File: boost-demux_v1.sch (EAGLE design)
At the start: 0 parts

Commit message: Lib updates + boost-demux design
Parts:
- added C1, C2: 4.7u, rcl:C-USC1206
- added C3: 100n, rcl:C-USC1206
- added C4: 10n, rcl:C-USC1206
- added C5: 22n, rcl:C-USC1206
- added C6: 1.8n, rcl:C-USC0805
- added C7: 27n, rcl:C-USC0805
- added C8, C9: 10u, rcl:C-USC1206
- added D1: FAIRCHILD_FSV8100V, components:FAIRCHILD_FSV8100V
- added L1: 4.7U, components:MURATA_FDVE1040
- added R1: 47k, rcl:R-US_R1206
- added R2: 1.37k, rcl:R-US_R0805
- added R3: 10k, rcl:R-US_R0805
- added R4: 154k, rcl:R-US_R0805
- added U1: TI_TPS55330, components:TI_TPS55330
- added U2, U3: (no value), SparkFun-PowerIC:ULN2803SOICW
- added U4: 4067D, 40xx:4067D
- added X1: (no value), pinhead:PINHD-2X8
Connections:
- new net +12V: C1.1, C2.1, C3.1, C4.1, L1.1, U1.EN, U1.VIN
- new net GND: C1.2, C2.2, C3.2, C4.2, C5.2, C6.2, C7.2, C8.2, C9.2, R1.1, R3.1, U1.AGND, U1.PAD, U1.PGND
- new net N$1: R1.2, U1.FREQ
- new net N$2: C5.1, U1.SS
- new net N$3: C6.1, R2.1, U1.COMP
- new net N$4: C7.1, R2.2
- new net N$5: R3.2, R4.1, U1.FB
- new net N$6: C8.1, C9.1, D1.C, R4.2
- new net N$7: D1.A, L1.2, U1.SW

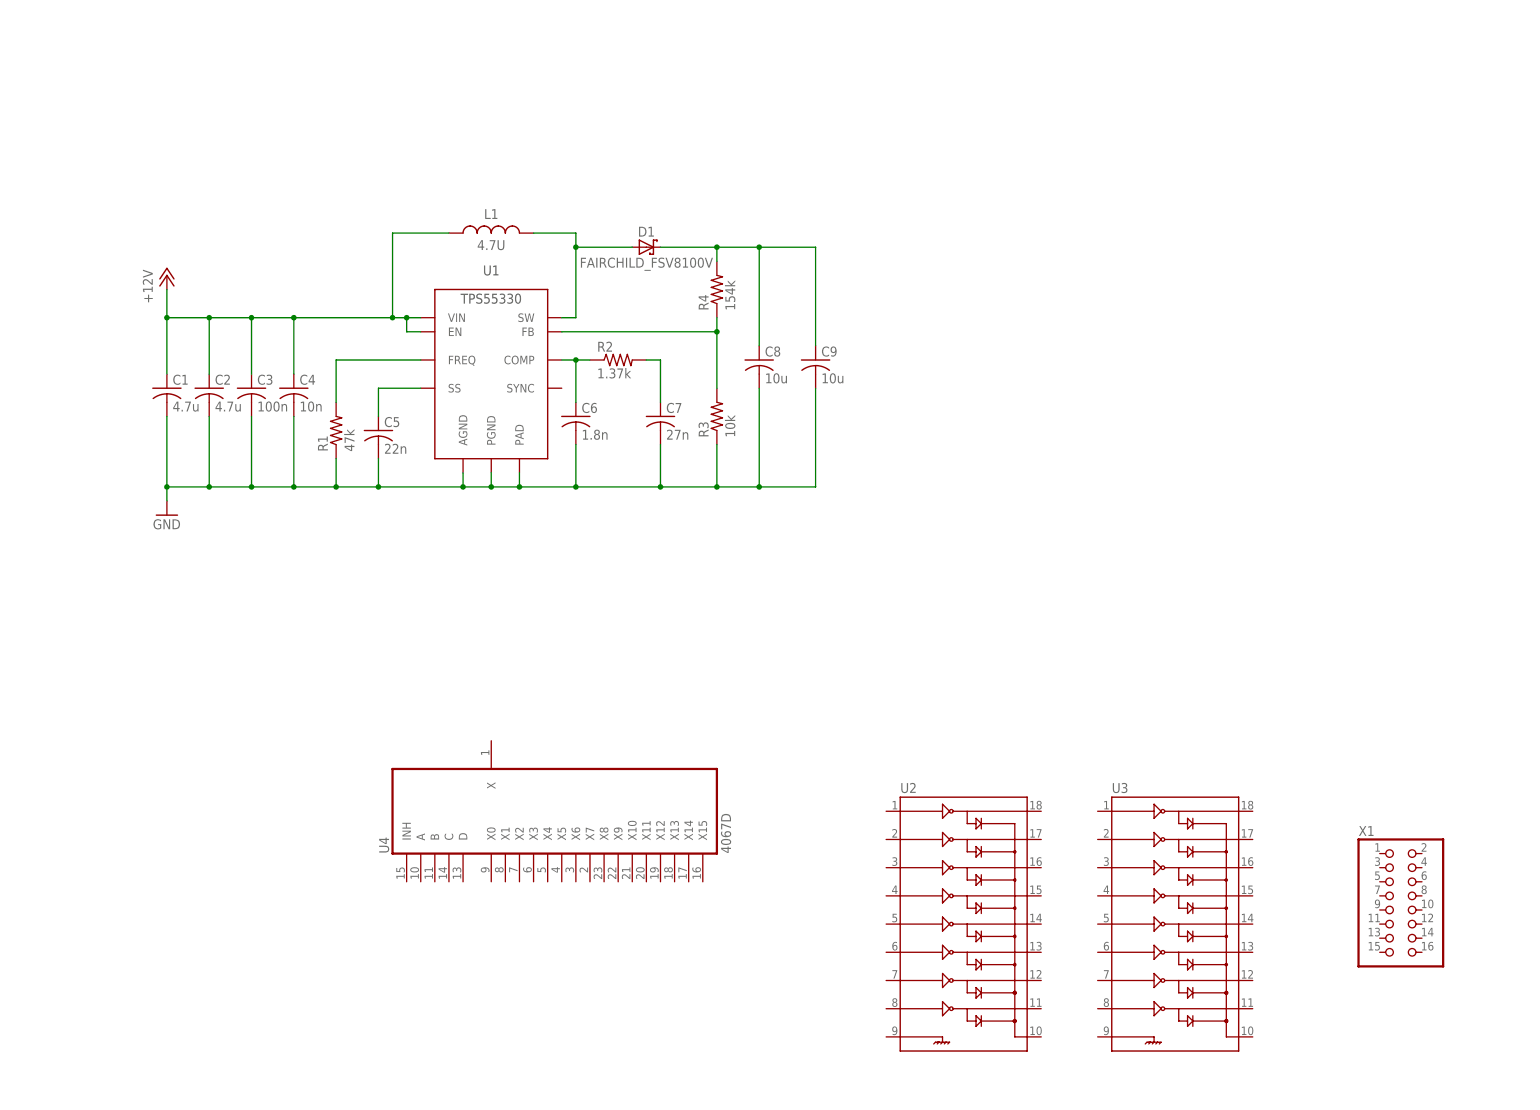
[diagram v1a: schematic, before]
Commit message: Slight update to boost-demux schematic
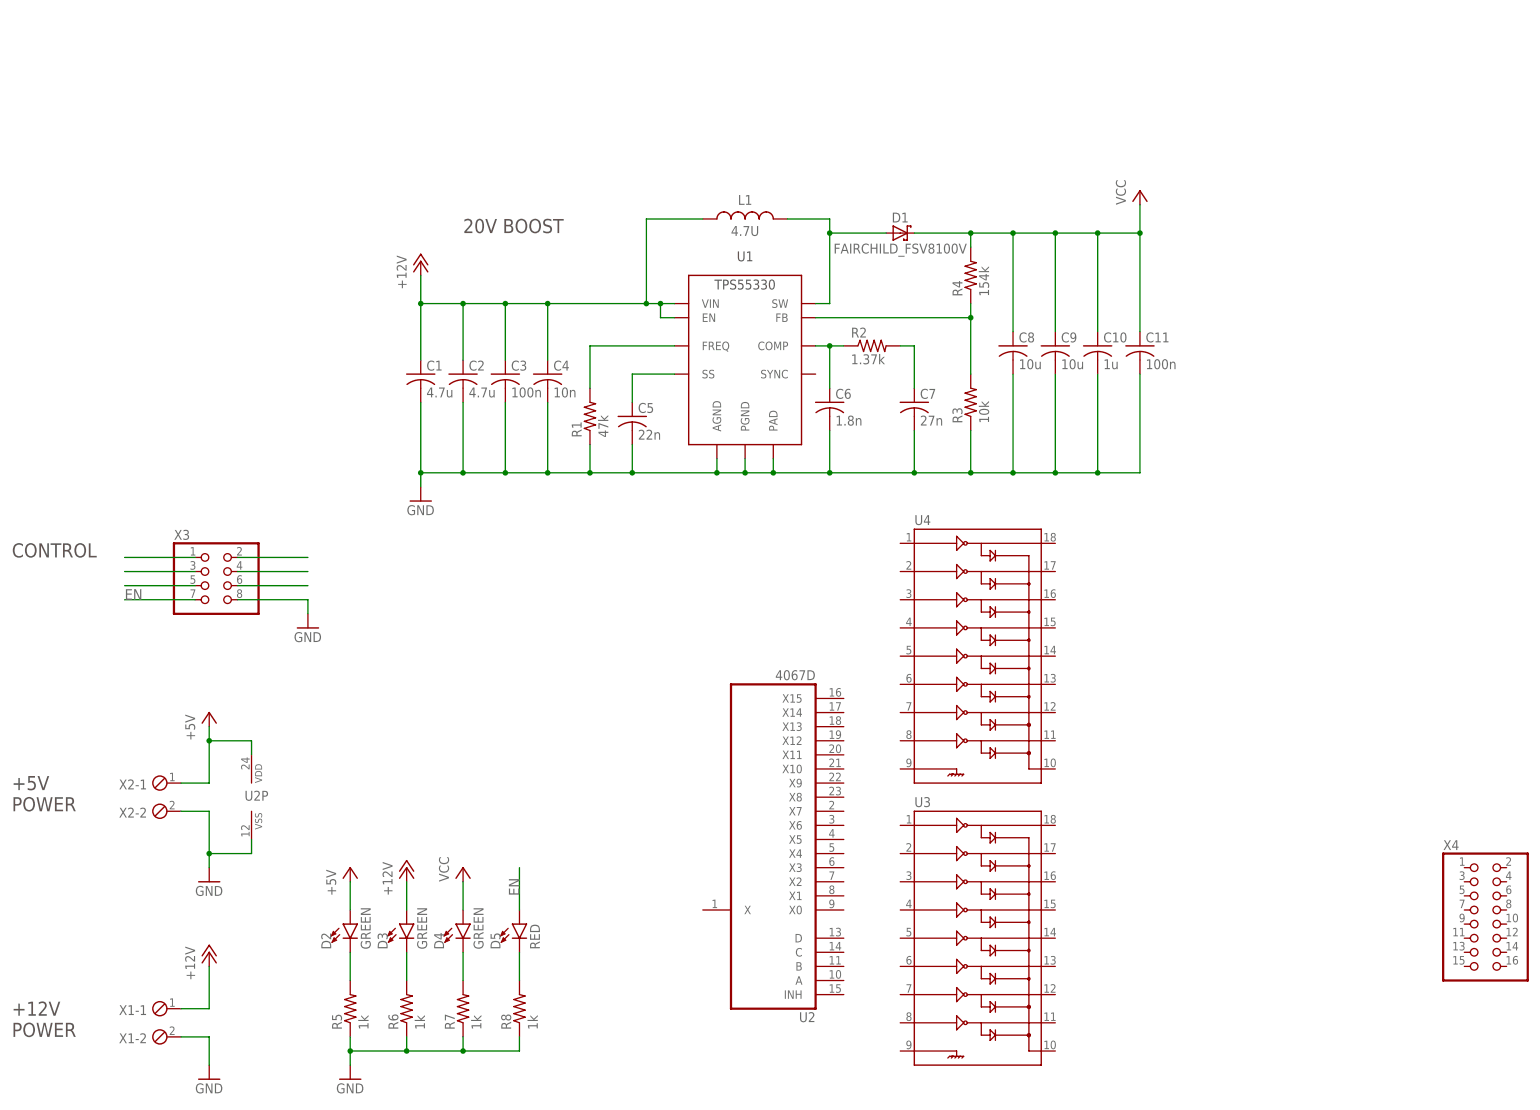
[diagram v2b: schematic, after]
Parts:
- added C10: 1u, rcl:C-USC1206
- added C11: 100n, rcl:C-USC1206
- added D2, D3, D4: GREEN, SparkFun-LED:LED5MM
- added D5: RED, SparkFun-LED:LED5MM
- added R5, R6, R7, R8: 1k, resistor:R-US_R1206
- added X2: (no value), con-phoenix-254:MPT2
- added X3: (no value), pinhead:PINHD-2X4/90
- added X4: (no value), pinhead:PINHD-2X8
- U2: value (none) -> 4067D; device SparkFun-PowerIC:ULN2803SOICW -> 40xx:4067D
- U4: value 4067D -> (none); device 40xx:4067D -> SparkFun-PowerIC:ULN2803SOICW
- X1: device pinhead:PINHD-2X8 -> con-phoenix-254:MPT2
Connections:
- new net +5V: D2.A, U2P.VDD, X2-1.1
- new net EN: D5.A, X3.7
- new net N$10: D5.C, R8.2
- new net N$11: X3.1
- new net N$14: X3.5
- new net N$15: X3.3
- new net N$16: X3.2
- new net N$17: X3.4
- new net N$18: X3.6
- new net N$8: D3.C, R6.2
- new net N$9: D4.C, R7.2
- new net VCC: C10.1, C11.1, C8.1, C9.1, D1.C, D4.A, R4.2
- net +12V: now also D3.A, X1-1.1
- net GND: now also C10.2, C11.2, R5.1, R6.1, R7.1, R8.1, U2P.VSS, X1-2.1, X2-2.1, X3.8
- net N$6: now also D2.C, R5.2; no longer C8.1, C9.1, D1.C, R4.2
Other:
- note added: "+12V POWER"
- note added: "+5V POWER"
- note added: "20V BOOST"
- note added: "CONTROL"
- moved on the sheet: C1, C2, C3, C4, C5, C6, C7, C8, C9, D1, L1, R1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

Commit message: PCB draft less markup
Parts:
- added C12: 100n, rcl:C-USC1206
- added D6: ON_FSV8100V, components:ON_FSV8100V
- added M1, M2, M3, M4: 6-32_MOUNT, components:6-32_MOUNT
- added Q1: ON_FDD4141, components:ON_FDD4141
- added R10, R11: 10k, rcl:R-US_R0805
- added R9: 470, resistor:R-US_R1206
- added U5: AVAGO_ACPL-217, components:AVAGO_ACPL-217
- added X5: (no value), pinhead:PINHD-2X8
- D1: value FAIRCHILD_FSV8100V -> ON_FSV8100V; device components:FAIRCHILD_FSV8100V -> components:ON_FSV8100V
- X2: device con-phoenix-254:MPT2 -> pinhead:PINHD-1X2/90
- X4: device pinhead:PINHD-2X8 -> pinhead:PINHD-1X3/90
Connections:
- new net A: U2A.A, X3.6
- new net B: U2A.B, X3.3
- new net C: U2A.C, X3.7
- new net D: U2A.D, X3.2
- new net N$12: C10.1, C11.1, C8.1, C9.1, D1.C, Q1.S, R10.1, R4.2
- new net N$13: Q1.G, R10.2, U5.P$4
- new net N$19: R9.1, U5.P$2
- new net N$20: U2A.X4, U3.4
- new net N$21: U2A.X5, U3.3
- new net N$22: U2A.X6, U3.2
- new net N$23: U2A.X7, U3.1
- new net N$24: U2A.X8, U4.8
- new net N$25: U2A.X9, U4.7
- new net N$26: U2A.X10, U4.6
- new net N$27: U2A.X11, U4.5
- new net N$28: U2A.X12, U4.4
- new net N$29: U2A.X13, U4.3
- new net N$30: U2A.X14, U4.2
- new net N$31: U2A.X15, U4.1
- new net N$32: U3.14, X5.3
- new net N$33: U3.15, X5.4
- new net N$34: U3.16, X5.5
- new net N$35: U3.17, X5.6
- new net N$36: U3.18, X5.7
- new net N$37: U4.11, X5.8
- new net N$38: U4.12, X5.9
- new net N$39: U4.13, X5.10
- new net N$40: U4.14, X5.11
- new net N$41: U4.15, X5.12
- new net STOP: X4.1, X5.15
- net +5V: now also C12.1, U2A.X, X3.4, X3.5, X5.14; no longer X2-1.1
- net EN: now also R11.2, U5.P$1, X2.1; no longer X3.7
- net GND: now also C12.2, D6.A, M1.P$1, M2.P$1, M3.P$1, M4.P$1, R11.1, R9.2, U2A.INH, U3.9, U4.9, U5.P$3, X2.2, X3.1, X4.3, X5.16; no longer X2-2.1
- net N$11: now also U2A.X0, U3.8; no longer X3.1
- net N$14: now also U3.12, X5.1; no longer X3.5
- net N$15: now also U2A.X1, U3.7; no longer X3.3
- net N$16: now also U2A.X2, U3.6; no longer X3.2
- net N$17: now also U2A.X3, U3.5; no longer X3.4
- net N$18: now also U3.13, X5.2; no longer X3.6
- net VCC: now also D6.C, Q1.D, U3.10, U4.10, X5.13; no longer C10.1, C11.1, C8.1, C9.1, D1.C, R4.2
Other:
- note added: "+20V BOOST"
- note added: "AUX"
- note added: "ENABLE"
- note added: "LOGIC ISOLATION"
- note added: "STOP"
- note removed: "+5V POWER"
- note removed: "20V BOOST"
- note removed: "CONTROL"
- moved on the sheet: C1, C10, C11, C2, C3, C4, C5, C6, C7, C8, C9, D1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

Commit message: Added minor PCB markup
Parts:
- D2: value GREEN -> +5V
- D3: value GREEN -> +12V
- D4: value GREEN -> +20V
- D5: value RED -> ENABLE
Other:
- note added: "GREEN"
- note added: "RED"
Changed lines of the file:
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@@
 <part name="C11" library="rcl" library_urn="urn:adsk.eagle:library:334" deviceset="C-US" device="C1206" value="100n"/>
 <part name="U2" library="40xx" library_urn="urn:adsk.eagle:library:80" deviceset="4067" device="D"/>
-<part name="D2" library="SparkFun-LED" deviceset="LED" device="5MM" value="GREEN"/>
-<part name="D3" library="SparkFun-LED" deviceset="LED" device="5MM" value="GREEN"/>
-<part name="D4" library="SparkFun-LED" deviceset="LED" device="5MM" value="GREEN"/>
+<part name="D2" library="SparkFun-LED" deviceset="LED" device="5MM" value="+5V"/>
+<part name="D3" library="SparkFun-LED" deviceset="LED" device="5MM" value="+12V"/>
+<part name="D4" library="SparkFun-LED" deviceset="LED" device="5MM" value="+20V"/>
 <part name="R5" library="resistor" library_urn="urn:adsk.eagle:library:348" deviceset="R-US_" device="R1206" value="1k"/>
 <part name="R6" library="resistor" library_urn="urn:adsk.eagle:library:348" deviceset="R-US_" device="R1206" value="1k"/>
@@
 <part name="GND4" library="supply1" library_urn="urn:adsk.eagle:library:371" deviceset="GND" device=""/>
 <part name="P+5" library="supply1" library_urn="urn:adsk.eagle:library:371" deviceset="+5V" device=""/>
-<part name="D5" library="SparkFun-LED" deviceset="LED" device="5MM" value="RED"/>
+<part name="D5" library="SparkFun-LED" deviceset="LED" device="5MM" value="ENABLE"/>
 <part name="R8" library="resistor" library_urn="urn:adsk.eagle:library:348" deviceset="R-US_" device="R1206" value="1k"/>
 <part name="P+6" library="supply1" library_urn="urn:adsk.eagle:library:371" deviceset="+12V" device=""/>
@@
 <text x="2.54" y="68.58" size="2.54" layer="97">ENABLE</text>
 <text x="2.54" y="109.22" size="2.54" layer="97">STOP</text>
+<text x="58.42" y="30.48" size="1.778" layer="97" rot="R90">GREEN</text>
+<text x="68.58" y="30.48" size="1.778" layer="97" rot="R90">GREEN</text>
+<text x="78.74" y="30.48" size="1.778" layer="97" rot="R90">GREEN</text>
+<text x="91.44" y="30.48" size="1.778" layer="97" rot="R90">RED</text>
 </plain>
 <instances>

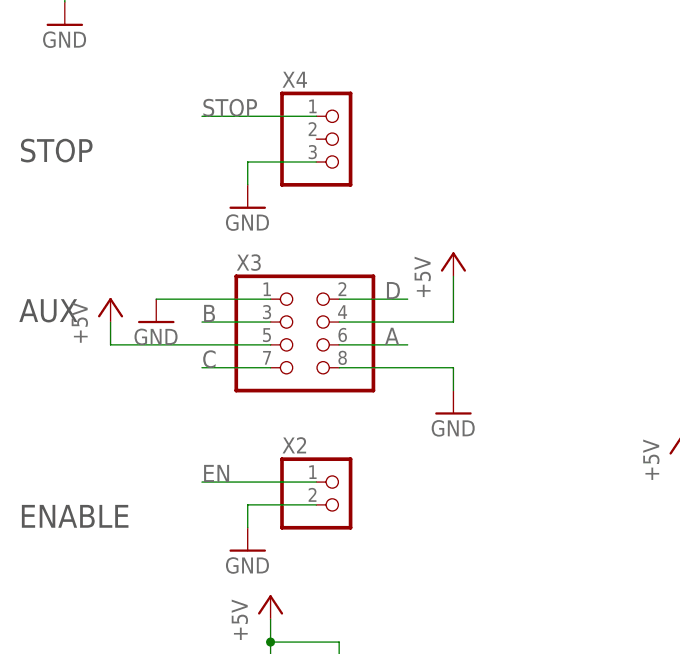
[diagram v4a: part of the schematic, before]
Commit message: Updates to boost-demux and FFC breakout
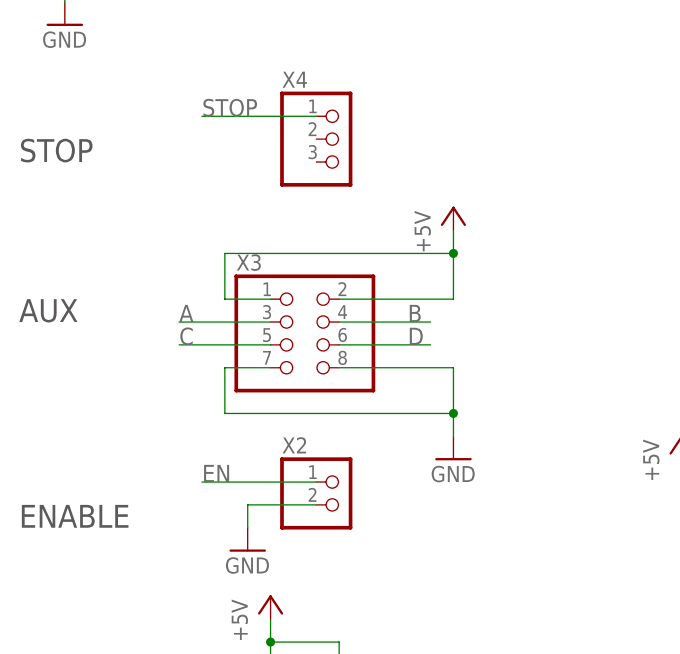
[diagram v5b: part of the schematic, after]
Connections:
- net +5V: now also X3.1, X3.2; no longer X3.4, X3.5
- net A: now also X3.3; no longer X3.6
- net B: now also X3.4; no longer X3.3
- net C: now also X3.5; no longer X3.7
- net D: now also X3.6; no longer X3.2
- net GND: now also X3.7; no longer X3.1, X4.3

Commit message: Logos
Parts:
- added LOGO1: MADOG, components:MADOG
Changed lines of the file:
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@@
 <part name="M3" library="components" deviceset="6-32_MOUNT" device=""/>
 <part name="M4" library="components" deviceset="6-32_MOUNT" device=""/>
+<part name="LOGO1" library="components" deviceset="MADOG" device=""/>
 </parts>
 <sheets>
@@
 <instance part="M3" gate="G$1" x="220.98" y="116.84"/>
 <instance part="M4" gate="G$1" x="220.98" y="111.76"/>
+<instance part="LOGO1" gate="G$1" x="12.7" y="43.18"/>
 </instances>
 <busses>
